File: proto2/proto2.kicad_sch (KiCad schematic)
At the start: 10 parts, among them J13 Daughter Card, SW1 SW_DIP_x04

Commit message: Final layout for 0.2.0 and various BOM and minor schematic updates.
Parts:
- BB1, J13: MPN (none) -> DNP
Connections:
- net VDD is gone; now on net +5V: J13.1 (Pin_1)
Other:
- note added: "GPIO_10"
- note added: "GPIO_110"
- note added: "GPIO_111"
- note added: "GPIO_32"
- note added: "GPIO_36"
- note added: "GPIO_62"
- note added: "GPIO_63"
- note added: "GPIO_71"
- note added: "GPIO_73"
- note added: "GPIO_74"
- note added: "GPIO_75"
- note added: "GPIO_76"
- note added: "GPIO_77"
- note added: "GPIO_8"
- note added: "GPIO_86"
- note added: "GPIO_87"
- note added: "GPIO_9"
- note added: "OUT_4 - OUT_7 WILL NOT WORK. NEED MMC PINS TO BOOT FROM."

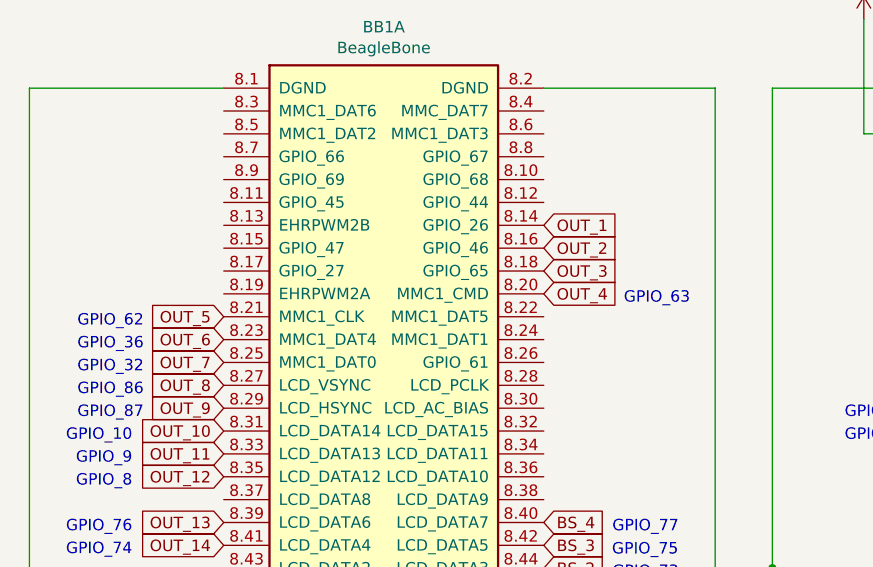
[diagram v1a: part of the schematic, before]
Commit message: Fixed SSR footprint in schematic and corrected output pinout.
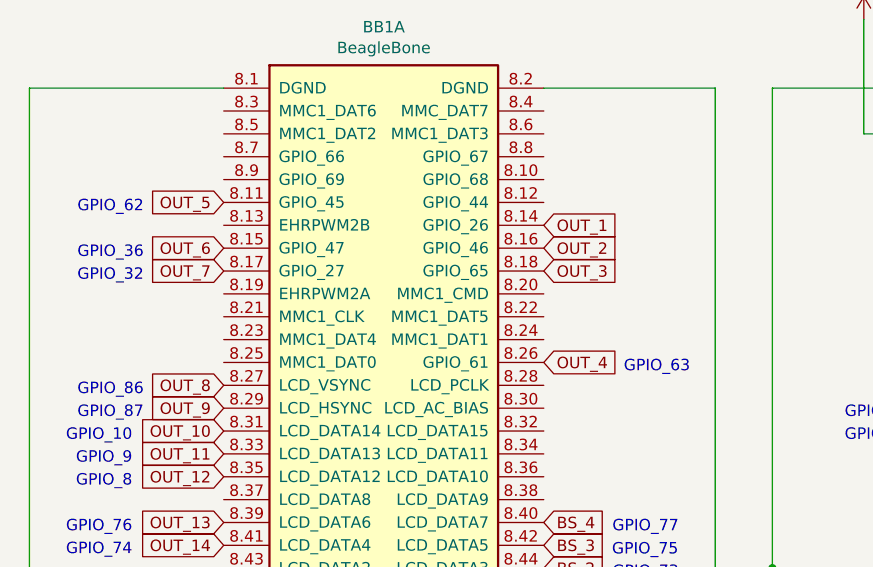
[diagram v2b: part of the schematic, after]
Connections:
- net OUT_4: now also BB1.8.26 (GPIO_61); no longer BB1.8.20 (MMC1_CMD)
- net OUT_5: now also BB1.8.11 (GPIO_45); no longer BB1.8.21 (MMC1_CLK)
- net OUT_6: now also BB1.8.15 (GPIO_47); no longer BB1.8.23 (MMC1_DAT4)
- net OUT_7: now also BB1.8.17 (GPIO_27); no longer BB1.8.25 (MMC1_DAT0)
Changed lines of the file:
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@@
   (title_block
     (title "Greenhouse 2.0 IO Board")
-    (date "2022-02-24")
+    (date "2022-03-06")
     (rev "0.2.0")
     (company "Langhe Greenhaus")
@@
     (effects (font (size 1.27 1.27)) (justify right bottom))
   )
-  (text "GPIO_32" (at 30.48 64.77 180)
+  (text "GPIO_32" (at 30.48 54.61 180)
     (effects (font (size 1.27 1.27)) (justify right bottom))
   )
@@
     (effects (font (size 1.27 1.27)) (justify right bottom))
   )
-  (text "GPIO_36" (at 30.48 62.23 180)
+  (text "GPIO_36" (at 30.48 52.07 180)
     (effects (font (size 1.27 1.27)) (justify right bottom))
   )
@@
     (effects (font (size 1.27 1.27)) (justify left bottom))
   )
-  (text "GPIO_63" (at 83.82 57.15 0)
+  (text "GPIO_63" (at 83.82 64.77 0)
     (effects (font (size 1.27 1.27)) (justify left bottom))
   )
@@
     (effects (font (size 1.27 1.27)) (justify left bottom))
   )
-  (text "GPIO_62" (at 30.48 59.69 180)
+  (text "GPIO_62" (at 30.48 46.99 180)
     (effects (font (size 1.27 1.27)) (justify right bottom))
   )
@@
     )
   )
-  (global_label "OUT_7" (shape input) (at 39.37 63.5 180) (fields_autoplaced)
+  (global_label "OUT_7" (shape input) (at 39.37 53.34 180) (fields_autoplaced)
     (effects (font (size 1.27 1.27)) (justify right))
-    (property "Intersheet References" "${INTERSHEET_REFS}" (id 0) (at 0 0 0)
+    (property "Intersheet References" "${INTERSHEET_REFS}" (id 0) (at 0 -10.16 0)
       (effects (font (size 1.27 1.27)) hide)
     )
@@
     )
   )
-  (global_label "OUT_4" (shape input) (at 74.93 55.88 0) (fields_autoplaced)
+  (global_label "OUT_4" (shape input) (at 74.93 63.5 0) (fields_autoplaced)
     (effects (font (size 1.27 1.27)) (justify left))
-    (property "Intersheet References" "${INTERSHEET_REFS}" (id 0) (at 114.3 0 0)
+    (property "Intersheet References" "${INTERSHEET_REFS}" (id 0) (at 114.3 7.62 0)
       (effects (font (size 1.27 1.27)) (justify left) hide)
     )
@@
     )
   )
-  (global_label "OUT_5" (shape input) (at 39.37 58.42 180) (fields_autoplaced)
+  (global_label "OUT_5" (shape input) (at 39.37 45.72 180) (fields_autoplaced)
     (effects (font (size 1.27 1.27)) (justify right))
-    (property "Intersheet References" "${INTERSHEET_REFS}" (id 0) (at 0 0 0)
+    (property "Intersheet References" "${INTERSHEET_REFS}" (id 0) (at 0 -12.7 0)
       (effects (font (size 1.27 1.27)) hide)
     )
@@
     )
   )
-  (global_label "OUT_6" (shape input) (at 39.37 60.96 180) (fields_autoplaced)
+  (global_label "OUT_6" (shape input) (at 39.37 50.8 180) (fields_autoplaced)
     (effects (font (size 1.27 1.27)) (justify right))
-    (property "Intersheet References" "${INTERSHEET_REFS}" (id 0) (at 0 0 0)
+    (property "Intersheet References" "${INTERSHEET_REFS}" (id 0) (at 0 -10.16 0)
       (effects (font (size 1.27 1.27)) hide)
     )
@@
     )
     (path "/00000000-0000-0000-0000-0000619eb5f5/00000000-0000-0000-0000-000061a298c2"
-      (reference "U1") (unit 1) (value "AQY282SX") (footprint "Package_SO:SO-4_4.4x4.3mm_P2.54mm")
+      (reference "U1") (unit 1) (value "AQY282SX") (footprint "JLCPCB:SO-4_6.0mm_P2.54mm")
     )
     (path "/00000000-0000-0000-0000-0000619eb5f5/00000000-0000-0000-0000-000061a3e24a"
-      (reference "U2") (unit 1) (value "AQY282SX") (footprint "Package_SO:SO-4_4.4x4.3mm_P2.54mm")
+      (reference "U2") (unit 1) (value "AQY282SX") (footprint "JLCPCB:SO-4_6.0mm_P2.54mm")
     )
     (path "/00000000-0000-0000-0000-0000619eb5f5/00000000-0000-0000-0000-000061b4d7b8"
-      (reference "U3") (unit 1) (value "AQY282SX") (footprint "Package_SO:SO-4_4.4x4.3mm_P2.54mm")
+      (reference "U3") (unit 1) (value "AQY282SX") (footprint "JLCPCB:SO-4_6.0mm_P2.54mm")
     )
     (path "/00000000-0000-0000-0000-0000619eb5f5/00000000-0000-0000-0000-000061a2c49b"
-      (reference "U4") (unit 1) (value "AQY282SX") (footprint "Package_SO:SO-4_4.4x4.3mm_P2.54mm")
+      (reference "U4") (unit 1) (value "AQY282SX") (footprint "JLCPCB:SO-4_6.0mm_P2.54mm")
     )
     (path "/00000000-0000-0000-0000-0000619eb5f5/00000000-0000-0000-0000-000061a3e49b"
-      (reference "U5") (unit 1) (value "AQY282SX") (footprint "Package_SO:SO-4_4.4x4.3mm_P2.54mm")
+      (reference "U5") (unit 1) (value "AQY282SX") (footprint "JLCPCB:SO-4_6.0mm_P2.54mm")
     )
     (path "/00000000-0000-0000-0000-0000619eb5f5/00000000-0000-0000-0000-000061b4dc7b"
-      (reference "U6") (unit 1) (value "AQY282SX") (footprint "Package_SO:SO-4_4.4x4.3mm_P2.54mm")
+      (reference "U6") (unit 1) (value "AQY282SX") (footprint "JLCPCB:SO-4_6.0mm_P2.54mm")
     )
     (path "/00000000-0000-0000-0000-0000619eb5f5/00000000-0000-0000-0000-000061a33784"
-      (reference "U7") (unit 1) (value "AQY282SX") (footprint "Package_SO:SO-4_4.4x4.3mm_P2.54mm")
+      (reference "U7") (unit 1) (value "AQY282SX") (footprint "JLCPCB:SO-4_6.0mm_P2.54mm")
     )
     (path "/00000000-0000-0000-0000-0000619eb5f5/00000000-0000-0000-0000-000061a3e4c4"
-      (reference "U8") (unit 1) (value "AQY282SX") (footprint "Package_SO:SO-4_4.4x4.3mm_P2.54mm")
+      (reference "U8") (unit 1) (value "AQY282SX") (footprint "JLCPCB:SO-4_6.0mm_P2.54mm")
     )
     (path "/00000000-0000-0000-0000-0000619eb5f5/00000000-0000-0000-0000-000061b4dc9e"
-      (reference "U9") (unit 1) (value "AQY282SX") (footprint "Package_SO:SO-4_4.4x4.3mm_P2.54mm")
+      (reference "U9") (unit 1) (value "AQY282SX") (footprint "JLCPCB:SO-4_6.0mm_P2.54mm")
     )
     (path "/00000000-0000-0000-0000-0000619eb5f5/00000000-0000-0000-0000-000061a351ca"
-      (reference "U10") (unit 1) (value "AQY282SX") (footprint "Package_SO:SO-4_4.4x4.3mm_P2.54mm")
+      (reference "U10") (unit 1) (value "AQY282SX") (footprint "JLCPCB:SO-4_6.0mm_P2.54mm")
     )
     (path "/00000000-0000-0000-0000-0000619eb5f5/00000000-0000-0000-0000-000061a3e4ed"
-      (reference "U11") (unit 1) (value "AQY282SX") (footprint "Package_SO:SO-4_4.4x4.3mm_P2.54mm")
+      (reference "U11") (unit 1) (value "AQY282SX") (footprint "JLCPCB:SO-4_6.0mm_P2.54mm")
     )
     (path "/00000000-0000-0000-0000-0000619eb5f5/00000000-0000-0000-0000-000061b4dcc1"
-      (reference "U12") (unit 1) (value "AQY282SX") (footprint "Package_SO:SO-4_4.4x4.3mm_P2.54mm")
+      (reference "U12") (unit 1) (value "AQY282SX") (footprint "JLCPCB:SO-4_6.0mm_P2.54mm")
     )
     (path "/00000000-0000-0000-0000-0000619eb5f5/3fbd0084-2e0c-4e1b-842b-cb1f6d5bdc95"
-      (reference "U13") (unit 1) (value "AQY282SX") (footprint "Package_SO:SO-4_4.4x4.3mm_P2.54mm")
+      (reference "U13") (unit 1) (value "AQY282SX") (footprint "JLCPCB:SO-4_6.0mm_P2.54mm")
     )
     (path "/00000000-0000-0000-0000-0000619eb5f5/b79f3646-42bf-4e1b-8d68-81901d398c74"
-      (reference "U14") (unit 1) (value "AQY282SX") (footprint "Package_SO:SO-4_4.4x4.3mm_P2.54mm")
+      (reference "U14") (unit 1) (value "AQY282SX") (footprint "JLCPCB:SO-4_6.0mm_P2.54mm")
     )
     (path "/3a9a5f1b-05d2-4421-a7ce-7632680b9874/6e05e766-0d4f-4396-82b4-9432f43bfe3e"

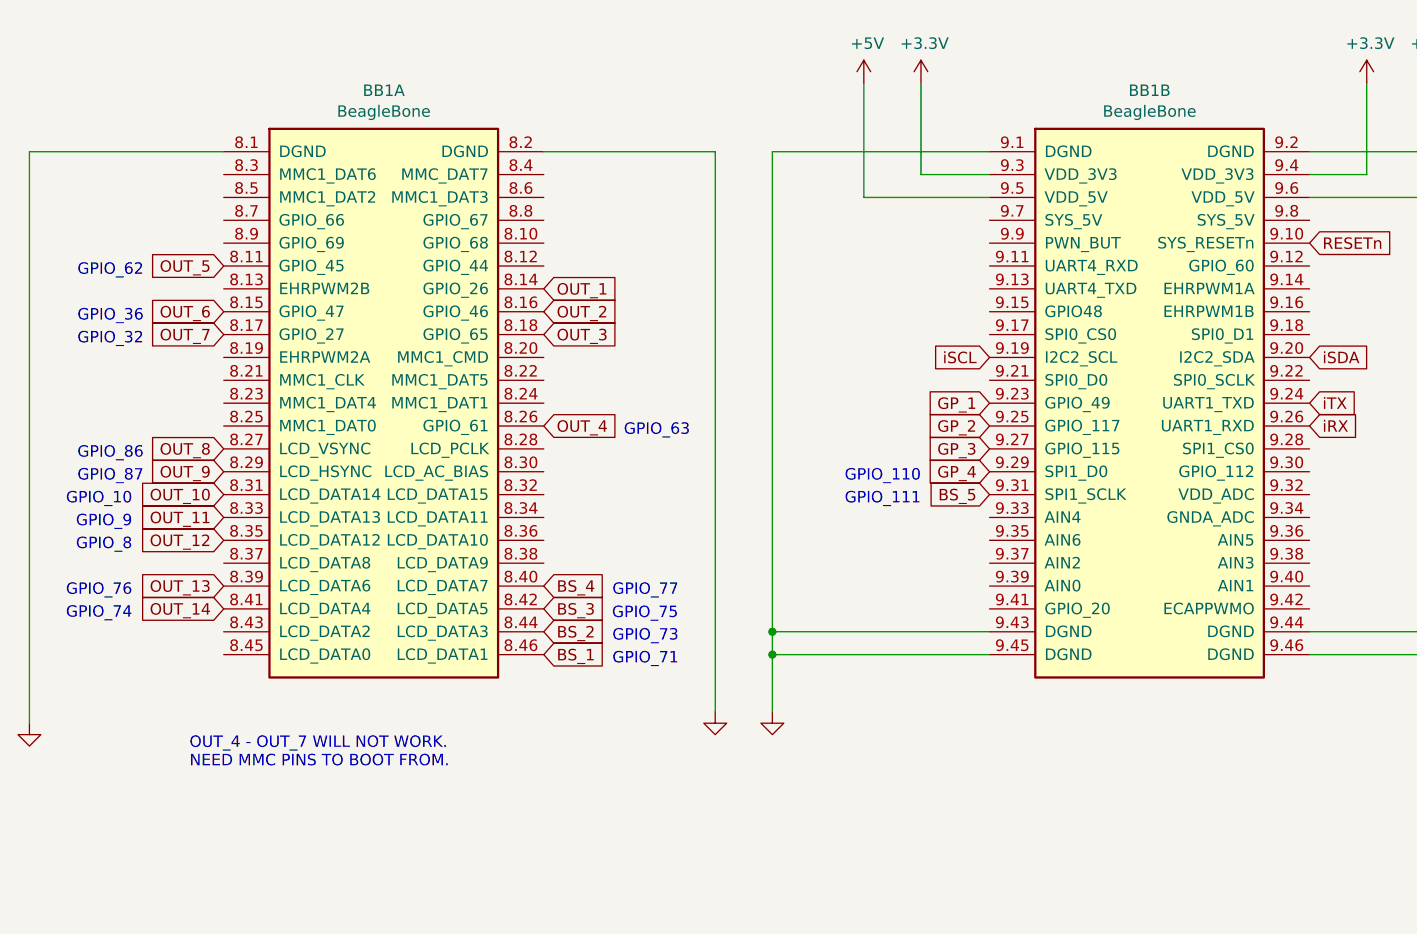
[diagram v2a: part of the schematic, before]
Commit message: Rearranged GPIO around the boot pins.
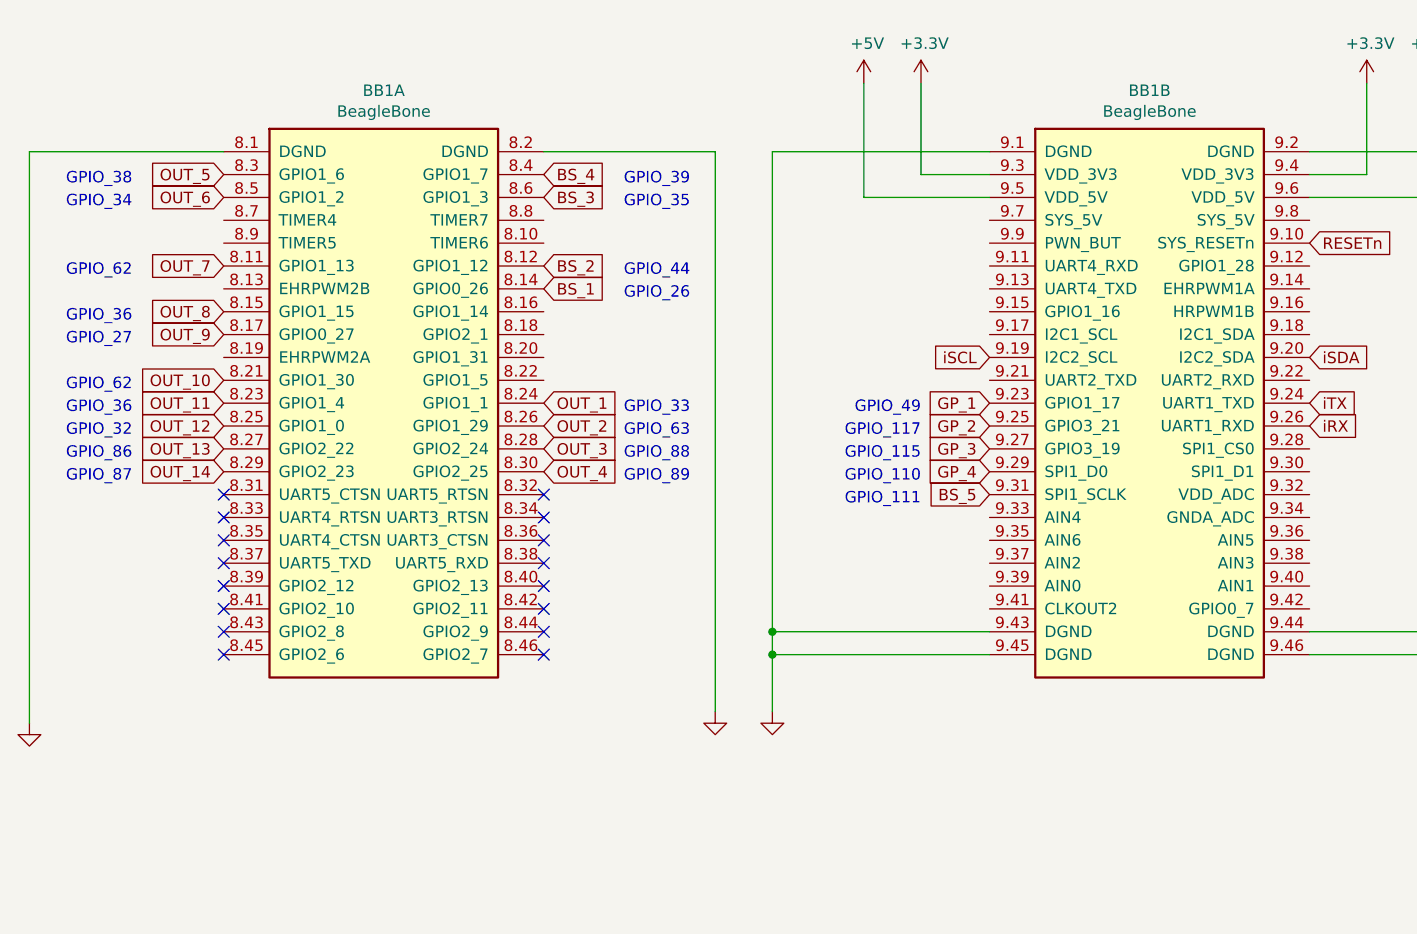
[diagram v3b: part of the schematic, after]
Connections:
- net BS_1: now also BB1.8.14 (GPIO0_26); no longer BB1.8.46 (LCD_DATA1)
- net BS_2: now also BB1.8.12 (GPIO1_12); no longer BB1.8.44 (LCD_DATA3)
- net BS_3: now also BB1.8.6 (GPIO1_3); no longer BB1.8.42 (LCD_DATA5)
- net BS_4: now also BB1.8.4 (GPIO1_7); no longer BB1.8.40 (LCD_DATA7)
- net OUT_1: now also BB1.8.24 (GPIO1_1); no longer BB1.8.14 (GPIO_26)
- net OUT_10: now also BB1.8.21 (GPIO1_30); no longer BB1.8.31 (LCD_DATA14)
- net OUT_11: now also BB1.8.23 (GPIO1_4); no longer BB1.8.33 (LCD_DATA13)
- net OUT_12: now also BB1.8.25 (GPIO1_0); no longer BB1.8.35 (LCD_DATA12)
- net OUT_13: now also BB1.8.27 (GPIO2_22); no longer BB1.8.39 (LCD_DATA6)
- net OUT_14: now also BB1.8.29 (GPIO2_23); no longer BB1.8.41 (LCD_DATA4)
- net OUT_2: now also BB1.8.26 (GPIO1_29); no longer BB1.8.16 (GPIO_46)
- net OUT_3: now also BB1.8.28 (GPIO2_24); no longer BB1.8.18 (GPIO_65)
- net OUT_4: now also BB1.8.30 (GPIO2_25); no longer BB1.8.26 (GPIO_61)
- net OUT_5: now also BB1.8.3 (GPIO1_6); no longer BB1.8.11 (GPIO_45)
- net OUT_6: now also BB1.8.5 (GPIO1_2); no longer BB1.8.15 (GPIO_47)
- net OUT_7: now also BB1.8.11 (GPIO1_13); no longer BB1.8.17 (GPIO_27)
- net OUT_8: now also BB1.8.15 (GPIO1_15); no longer BB1.8.27 (LCD_VSYNC)
- net OUT_9: now also BB1.8.17 (GPIO0_27); no longer BB1.8.29 (LCD_HSYNC)
- no-connect marks 0 -> 16
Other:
- note added: "GPIO_115"
- note added: "GPIO_117"
- note added: "GPIO_26"
- note added: "GPIO_27"
- note added: "GPIO_33"
- note added: "GPIO_34"
- note added: "GPIO_35"
- note added: "GPIO_38"
- note added: "GPIO_39"
- note added: "GPIO_44"
- note added: "GPIO_49"
- note added: "GPIO_88"
- note added: "GPIO_89"
- note removed: "GPIO_10"
- note removed: "GPIO_71"
- note removed: "GPIO_73"
- note removed: "GPIO_74"
- note removed: "GPIO_75"
- note removed: "GPIO_76"
- note removed: "GPIO_77"
- note removed: "GPIO_8"
- note removed: "GPIO_9"
- note removed: "OUT_4 - OUT_7 WILL NOT WORK. NEED MMC PINS TO BOOT FROM."
